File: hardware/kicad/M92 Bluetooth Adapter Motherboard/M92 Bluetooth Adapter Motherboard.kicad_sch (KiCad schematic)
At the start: 27 parts, among them IC1 PIC18F27Q43-I/SO, J2 Conn_Handset_RJ45, J6 Conn_MCU_Programming, J7 Conn_BT_Module, J8 Conn_MCU_IO_UART, Q2 PN2222ATA

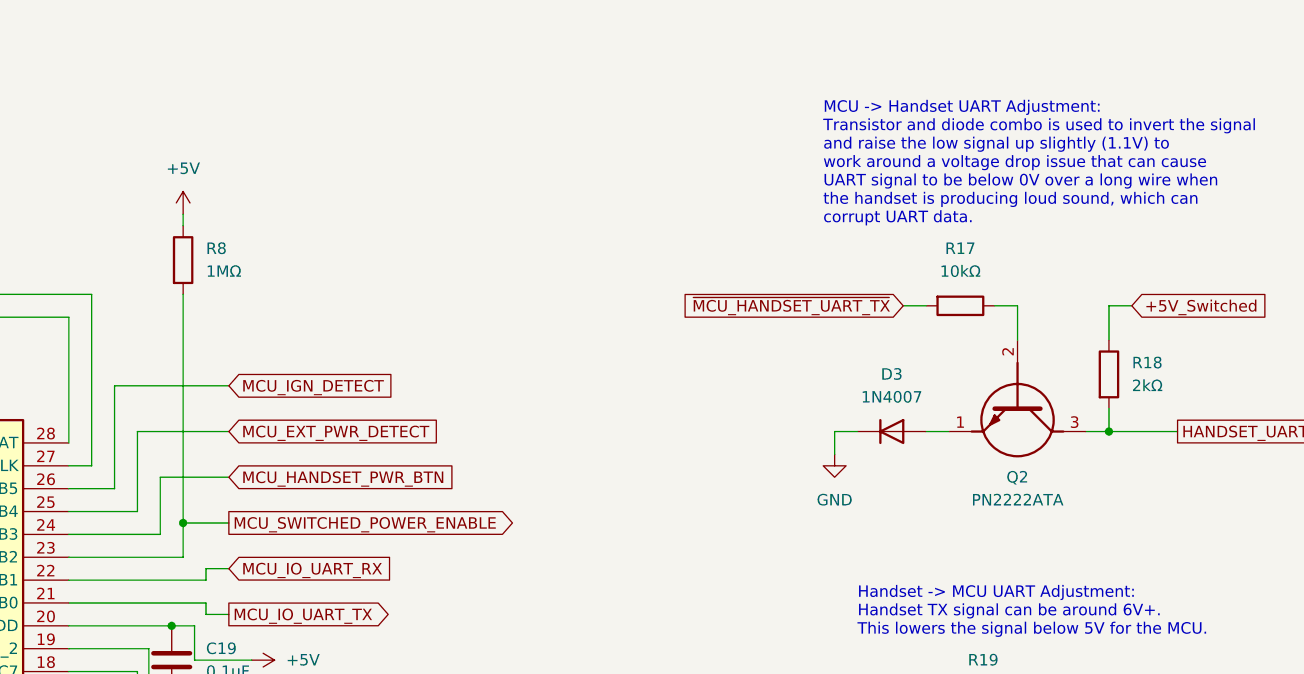
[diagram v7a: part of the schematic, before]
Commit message: Rework load switch enable circuitry/code
Rework load switch enable circuitry/code to fix brief power-on glitch when initially connecting battery power.
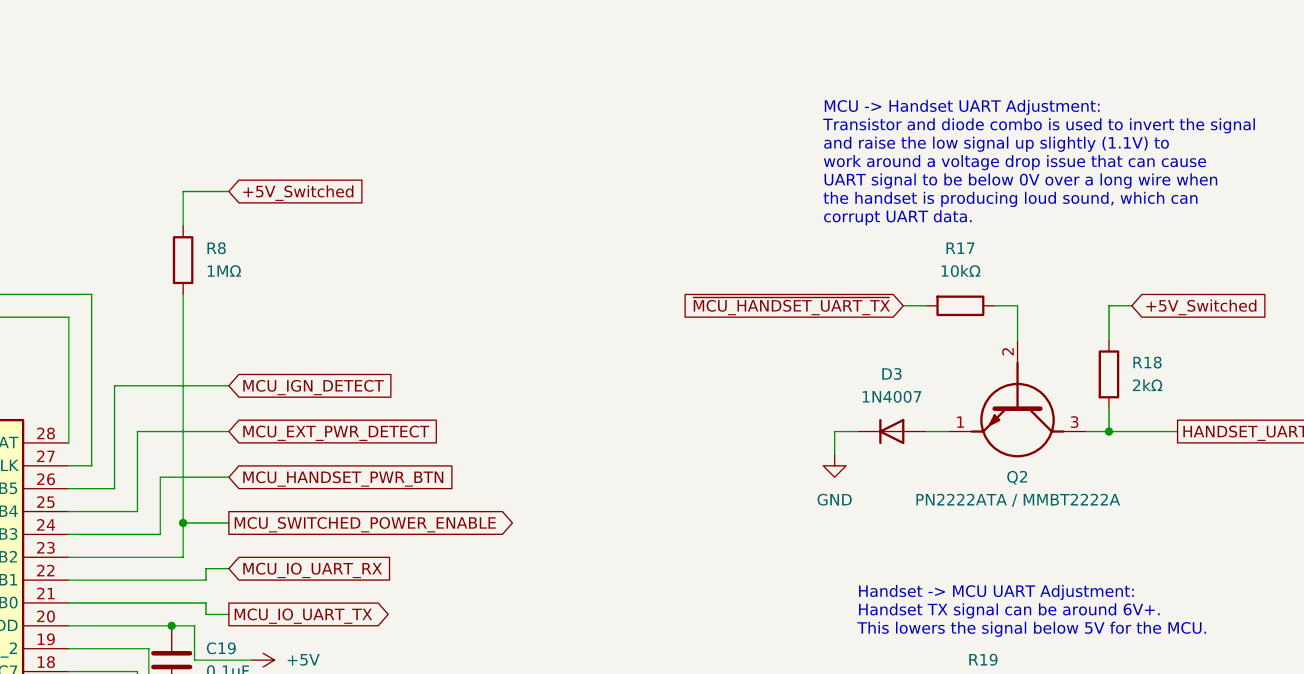
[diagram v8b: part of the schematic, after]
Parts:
- Q2: value PN2222ATA -> PN2222ATA / MMBT2222A
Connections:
- net +5V: no longer R8.1
- net +5V_Switched: now also R8.1
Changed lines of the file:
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@@
     (stroke (width 0) (type default))
   )
-  (wire (pts (xy 137.16 29.21) (xy 137.16 30.48))
+  (wire (pts (xy 137.16 26.67) (xy 137.16 30.48))
     (stroke (width 0) (type default))
   )
@@
   )
   (wire (pts (xy 134.62 148.59) (xy 143.51 148.59))
+    (stroke (width 0) (type default))
+  )
+  (wire (pts (xy 142.24 26.67) (xy 137.16 26.67))
     (stroke (width 0) (type default))
   )
@@
     (effects (font (size 1.27 1.27)) (justify left))
     (property "Intersheetrefs" "${INTERSHEET_REFS}" (at 162.8237 158.75 0)
+      (effects (font (size 1.27 1.27)) (justify left))
+    )
+  )
+  (global_label "+5V_Switched" (shape input) (at 142.24 26.67 0) (fields_autoplaced)
+    (effects (font (size 1.27 1.27)) (justify left))
+    (property "Intersheetrefs" "${INTERSHEET_REFS}" (at 158.409 26.67 0)
       (effects (font (size 1.27 1.27)) (justify left))
     )
@@
       (effects (font (size 1.27 1.27)))
     )
-    (property "Value" "PN2222ATA" (at 229.87 60.96 90)
+    (property "Value" "PN2222ATA / MMBT2222A" (at 229.87 60.96 90)
       (effects (font (size 1.27 1.27)))
     )
@@
         )
       )
-    )
-  )
-  (symbol (lib_id "power:+5V") (at 137.16 29.21 0) (unit 1)
-    (in_bom yes) (on_board yes) (dnp no) (fields_autoplaced)
-    (property "Reference" "#PWR041" (at 137.16 33.02 0)
-      (effects (font (size 1.27 1.27)) hide)
-    )
-    (property "Value" "+5V" (at 137.16 24.13 0)
-      (effects (font (size 1.27 1.27)))
-    )
-    (property "Footprint" "" (at 137.16 29.21 0)
-      (effects (font (size 1.27 1.27)) hide)
-    )
-    (property "Datasheet" "" (at 137.16 29.21 0)
-      (effects (font (size 1.27 1.27)) hide)
-    )
-    (pin "1")
-    (instances
-      (project "M92 Bluetooth Adapter Motherboard"
-        (path "/d695ac67-4f6c-46c1-9ce6-2d543d3b66ce"
-          (reference "#PWR041") (unit 1)
-        )
-      )
